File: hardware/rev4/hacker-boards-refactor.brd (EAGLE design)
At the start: 25.4 x 58.4 mm, 38 parts, among them J1 MICRO_USB_B_JST_MC5BR3-M404-4S

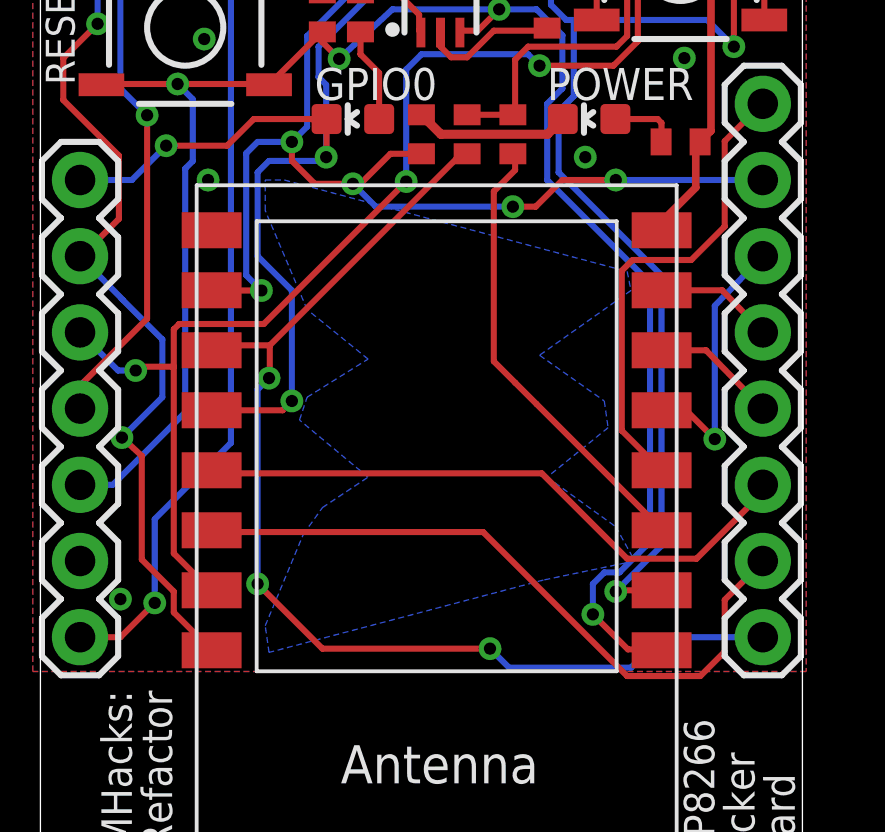
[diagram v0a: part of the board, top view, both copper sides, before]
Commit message: Updated logo, small fixes on artwork
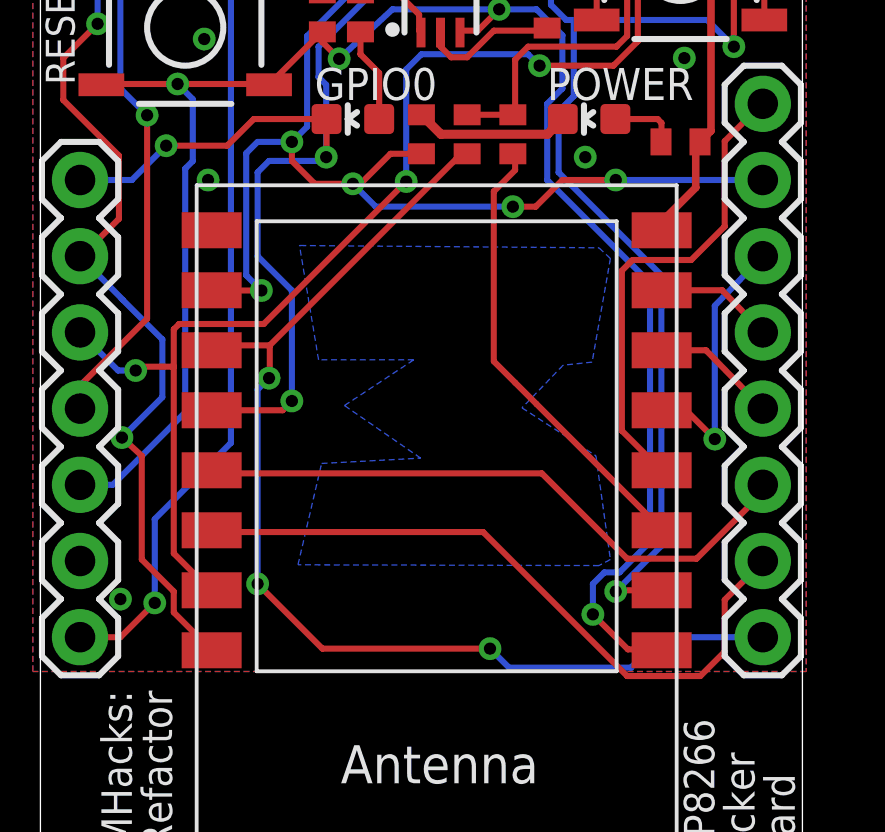
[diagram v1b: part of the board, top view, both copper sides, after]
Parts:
- U$1: device hacker-board:EDGY-LOGO-TRACES -> hacker-board:LOGO8EDGY
- moved U$1 3.91 mm to (8.69, 12.1)
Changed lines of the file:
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@@
 <setting verticaltext="up"/>
 </settings>
-<grid distance="5" unitdist="mil" unit="mil" style="lines" multiple="1" display="yes" altdistance="0.001" altunitdist="inch" altunit="inch"/>
+<grid distance="1" unitdist="mil" unit="mil" style="lines" multiple="1" display="yes" altdistance="0.001" altunitdist="inch" altunit="inch"/>
 <layers>
 <layer number="1" name="Top" color="4" fill="1" visible="yes" active="yes"/>
@@
 <attribute name="VALUE" x="20.9042" y="28.702" size="1.27" layer="27" rot="R270"/>
 </element>
-<element name="U$1" library="hacker-board" package="EDGY-LOGO-TRACES" value="" x="6.858" y="8.636" rot="MR90"/>
+<element name="U$1" library="hacker-board" package="LOGO8EDGY" value="" x="8.6868" y="12.0904" rot="MR90"/>
 </elements>
 <signals>
@@
 <signal name="N$2">
 <polygon width="0.2032" layer="16">
-<vertex x="8.128" y="24.892"/>
-<vertex x="19.558" y="21.844"/>
-<vertex x="19.685" y="21.209"/>
-<vertex x="16.637" y="19.05"/>
-<vertex x="18.796" y="17.526"/>
-<vertex x="18.923" y="16.637"/>
-<vertex x="16.891" y="14.986"/>
-<vertex x="19.177" y="13.335"/>
-<vertex x="19.812" y="12.192"/>
-<vertex x="16.764" y="11.557"/>
-<vertex x="7.62" y="9.144"/>
-<vertex x="7.493" y="10.033"/>
-<vertex x="8.763" y="13.081"/>
-<vertex x="9.398" y="13.97"/>
-<vertex x="10.922" y="14.986"/>
-<vertex x="8.636" y="16.891"/>
-<vertex x="8.89" y="17.653"/>
-<vertex x="10.922" y="18.923"/>
-<vertex x="8.89" y="20.574"/>
-<vertex x="7.493" y="23.876"/>
-<vertex x="7.493" y="24.892"/>
+<vertex x="8.6614" y="22.7076"/>
+<vertex x="18.6182" y="22.6314"/>
+<vertex x="18.9992" y="22.2758"/>
+<vertex x="18.3896" y="18.8214"/>
+<vertex x="17.4244" y="18.7198"/>
+<vertex x="16.0528" y="17.2974"/>
+<vertex x="18.5166" y="15.6972"/>
+<vertex x="18.9992" y="12.2428"/>
+<vertex x="18.6182" y="12.0396"/>
+<vertex x="8.5852" y="12.065"/>
+<vertex x="9.3726" y="15.4432"/>
+<vertex x="12.6746" y="15.621"/>
+<vertex x="10.1346" y="17.3736"/>
+<vertex x="12.446" y="18.8976"/>
+<vertex x="9.271" y="18.8976"/>
+<vertex x="8.636" y="22.7076"/>
 </polygon>
 </signal>

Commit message: Tiny routing changes to make DRC happy
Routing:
- net DTR: track 46.5 -> 42.5 mm
- net TX: track 55.7 -> 56.3 mm
- net GND: vias 27 -> 28
